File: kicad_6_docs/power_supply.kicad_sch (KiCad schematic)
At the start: 54 parts, among them J4 iec_power_entry, SW4 SW_SPST, T1 power_transformer, U1 NE5532, U10 TL072, U11 TL072, U12 SSI2164, U13 TL072, U14 TL072, U15 TL072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

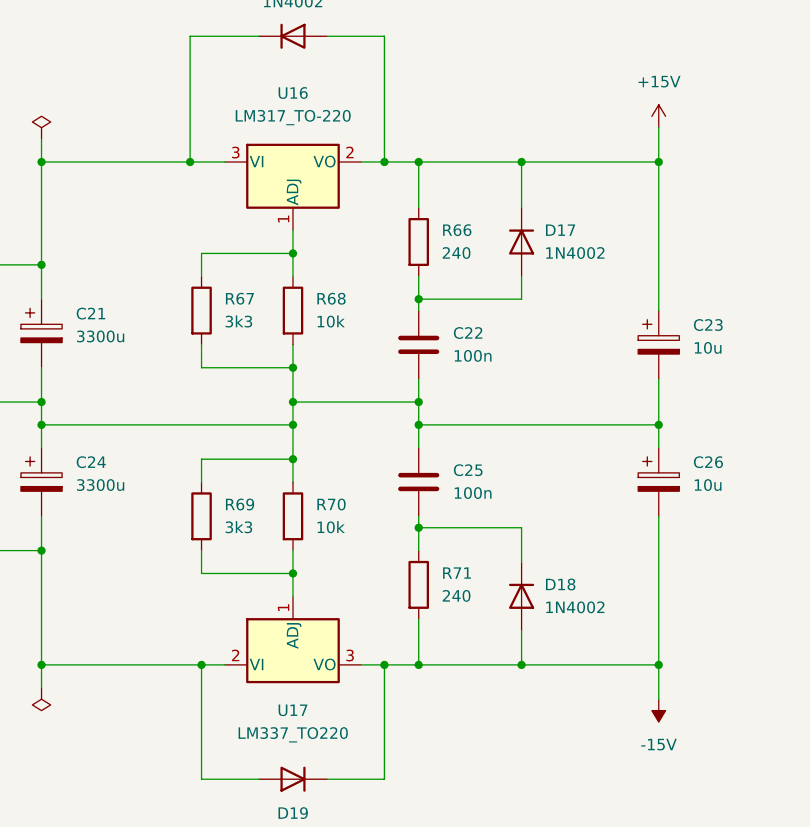
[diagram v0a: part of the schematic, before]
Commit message: Fix power supply errors, tidy up schematic
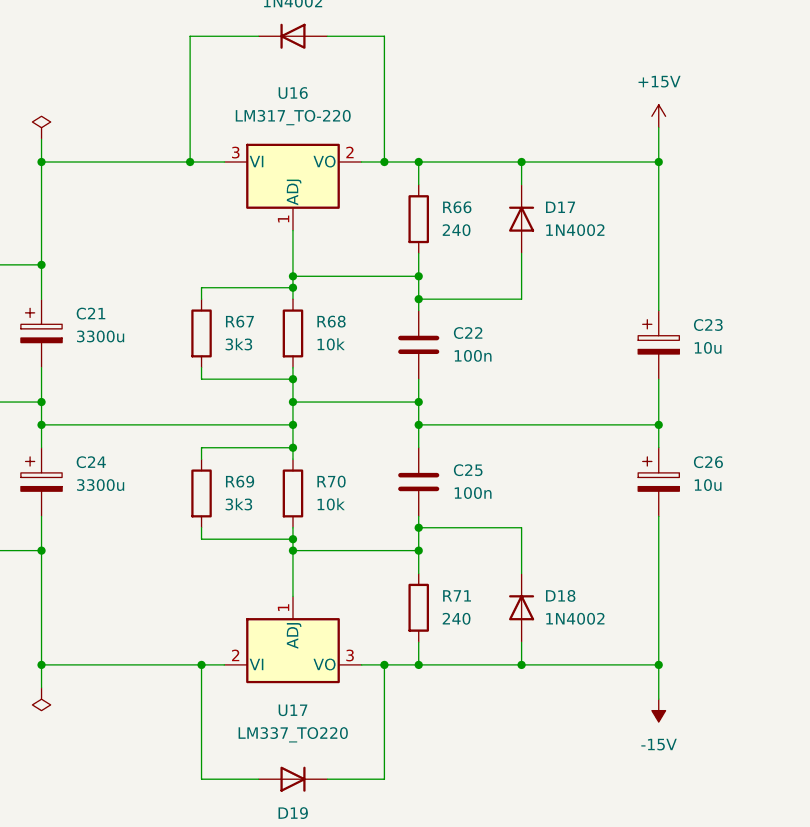
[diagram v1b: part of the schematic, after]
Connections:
- net at R67.1, R68.1, U16.1 (ADJ): now also C22.1, D17.2 (A), R66.2
- net at C25.2, D18.1 (K), R71.1: now also R69.2, R70.2, U17.1 (ADJ)
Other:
- moved on the sheet: D17, D18, R66, R67, R68, R69, R70, R71
